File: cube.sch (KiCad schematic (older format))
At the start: 20 parts, among them J1 serial_conn, J10 Conn_01x01, J11 Conn_01x01, J2 shifters_common_conn, J3 Conn_01x01, J4 Conn_01x01, J5 Conn_01x01, J6 Conn_01x01, J7 Conn_01x01, J8 Conn_01x01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

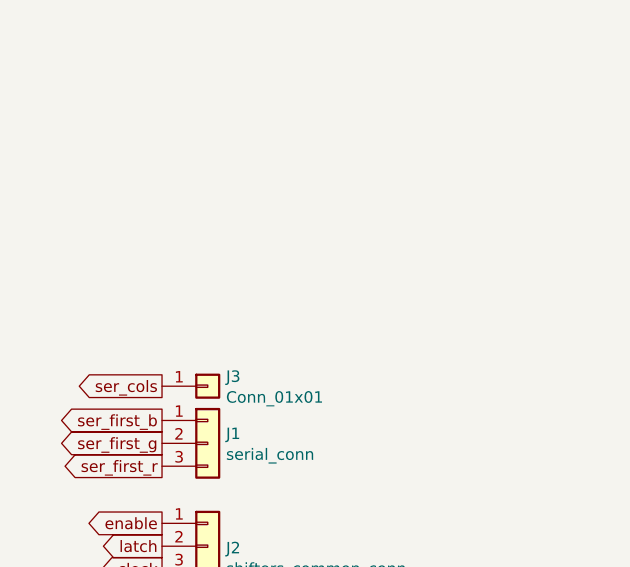
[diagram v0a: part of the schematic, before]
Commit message: connect power and fix unconnected
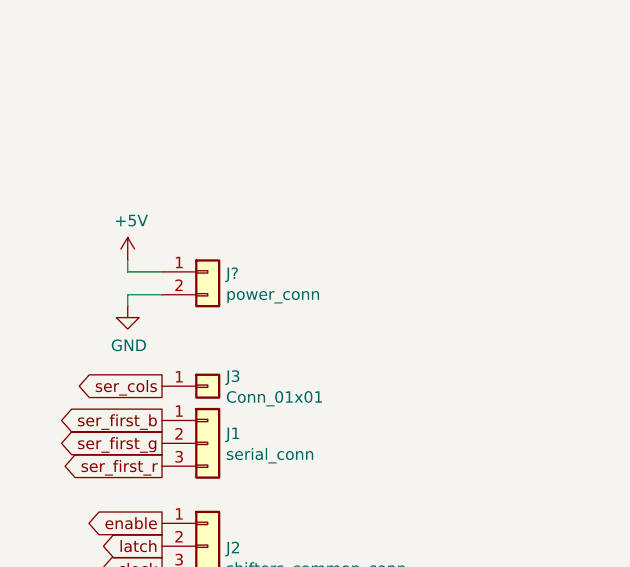
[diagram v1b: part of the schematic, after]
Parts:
- added J?: power_conn, symbol Connector_Generic:Conn_01x02
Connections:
- net +5V: now also J?.1 (Pin_1)
- net GND: now also J?.2 (Pin_2)
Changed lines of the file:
@@
 	1    0    0    -1
 $EndComp
+$Comp
+L Connector_Generic:Conn_01x02 J?
+U 1 1 5FB3C853
+P 1500 14000
+F 0 "J?" H 1580 13992 50  0000 L CNN
+F 1 "power_conn" H 1580 13901 50  0000 L CNN
+F 2 "" H 1500 14000 50  0001 C CNN
+F 3 "~" H 1500 14000 50  0001 C CNN
+	1    1500 14000
+	1    0    0    -1
+$EndComp
+$Comp
+L power:+5V #PWR?
+U 1 1 5FB3D000
+P 1150 13950
+F 0 "#PWR?" H 1150 13800 50  0001 C CNN
+F 1 "+5V" H 1165 14123 50  0000 C CNN
+F 2 "" H 1150 13950 50  0001 C CNN
+F 3 "" H 1150 13950 50  0001 C CNN
+	1    1150 13950
+	1    0    0    -1
+$EndComp
+Wire Wire Line
+	1150 13950 1150 14000
+Wire Wire Line
+	1150 14000 1300 14000
+$Comp
+L power:GND #PWR?
+U 1 1 5FB3E3BB
+P 1150 14150
+F 0 "#PWR?" H 1150 13900 50  0001 C CNN
+F 1 "GND" H 1155 13977 50  0000 C CNN
+F 2 "" H 1150 14150 50  0001 C CNN
+F 3 "" H 1150 14150 50  0001 C CNN
+	1    1150 14150
+	1    0    0    -1
+$EndComp
+Wire Wire Line
+	1150 14150 1150 14100
+Wire Wire Line
+	1150 14100 1300 14100
 $EndSCHEMATC
